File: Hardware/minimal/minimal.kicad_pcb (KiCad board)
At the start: 4 copper layers, 48 x 35 mm, 95 parts, among them J101 USB_C_Receptacle_USB2.0_16P, J301 AudioJack3_SwitchTR, J302 AudioJack3_SwitchTR, SW101 SW_SPST, U101 KTM1331TD-ST3, U102 USBLC6-2P6, U103 TLV76733DRVx, U104 TLV76733DRVx, U301 OPA2323, U302 TAC5242, U401 APS6404L-3SQRx-ZR, U402 RP2354A, Y401 ABM8-272-T3

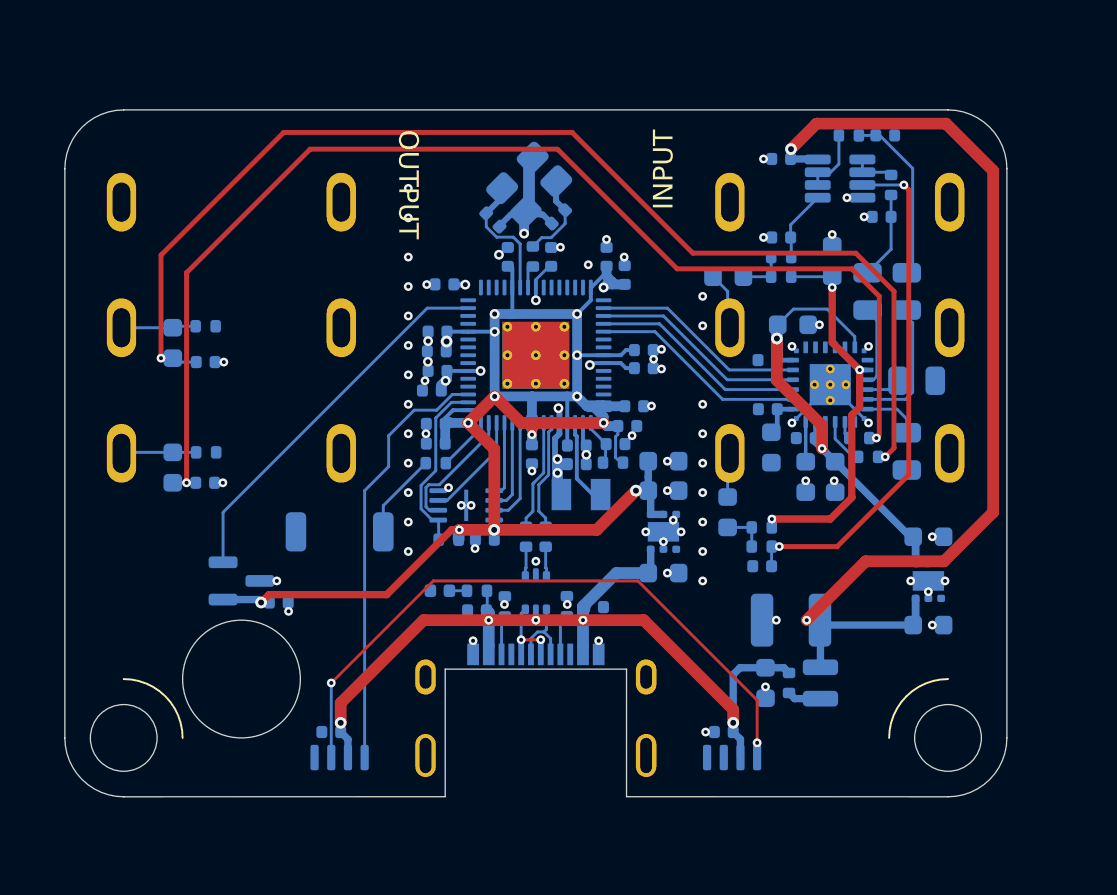
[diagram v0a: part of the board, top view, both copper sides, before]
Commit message: Commit DC-coupled TAC5112 design
This is a slightly modified 'minimal' board with the same board outline
but an added 3.5mm DC jack.

The upside: no coupling capacitors into the codec that have distortion
at low-end frequencies due to the capacitors' voltage coefficients.  The
existing 0805 4.7uF caps were large for this minimal board, and caused
the THD+N to go to roughly -65dB for a low-B bass signal at a reasonable
signal level of 0.1Vrms.  That's not horrible, but it's not optimal.

The 10Hz corner also caused issues for using the pedal as a measurement
instrument, since it introduced a consistent measurement error that was
initially incorrectly attributed to the pedal under test.

The other upside is simply the existence of the headphone jack.  That
user-visible addition is likely a lot more noticeable than the
low-frequency THD+N improvement this should bring or the improvement in
low-end frequency response.

Downside: the TAC212 with a better noise floor is out of stock, and so I
am back to the slightly lower dynamic range of the TAC5112 - but with
the new fixed footprint with proper paste and thermal vias.  The thermal
pad is likely to actually come into play now that the codec is used as a
headphone amplifier too.

The lower dynamic range is unlikely to be noticeable - it wasn't on the
original mono boards (the added noise was probably entirely due to the
negative inputs having been left floating on that board).

And I'll need to route i2c again, and it's an entirely new untested
configuration.  I've added a trace to route one of the TAC5112 GPIOs
just in case it comes in useful - possibly as an ASI error reporting
interrupt line.

The default codec routing for that new pin being routed is as an
interrupt output: driven low with a weak pull-up.  It's routed to GPIO15
on the rp2354, which hardware in turn defaults to a weak pull-down,
disconnected from any logic.

So without any firmware, this ends up being a few microamps of current
on that trace due to the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
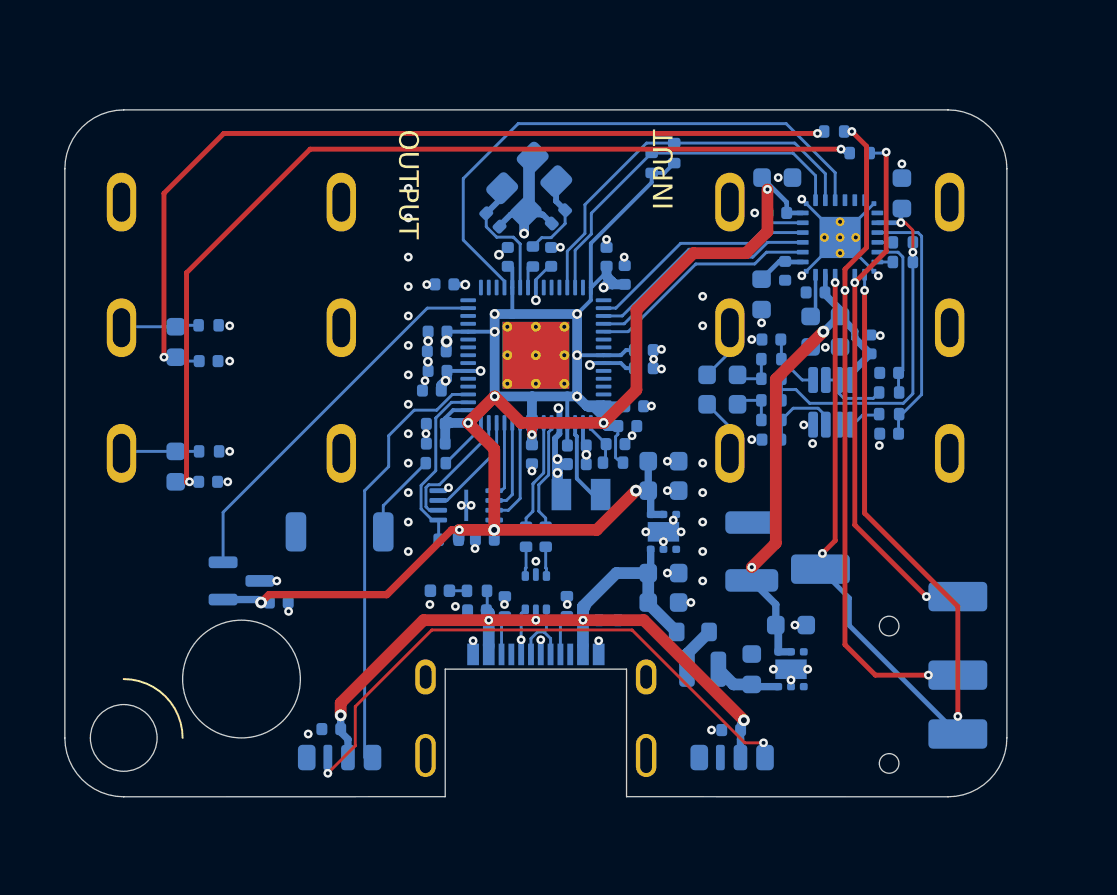
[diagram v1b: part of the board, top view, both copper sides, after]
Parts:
- removed C312, C313, C314, C315: 4.7uF, Capacitor_SMD:C_0805_2012Metric
- added J303: AudioJack4, Mylib:PJ-320D, B.Cu at (118.0, 135.0)
- added R105: 5k1, Resistor_SMD:R_0402_1005Metric, B.Cu at (105.9, 102.7)
- added R106: 5k1, Resistor_SMD:R_0402_1005Metric, B.Cu at (107.0, 102.2)
- added R312: 100R, Resistor_SMD:R_0402_1005Metric, B.Cu at (118.7, 107.8)
- added R313: 100R, Resistor_SMD:R_0402_1005Metric, B.Cu at (118.7, 106.8)
- D102, D103: value WS2812B-4020 -> WS2812B-4020-V6; footprint Mylib:WS2812B-4020 -> Mylib:WS2812B-4020-V6
- R104: value 10R -> 1R; footprint Resistor_SMD:R_0402_1005Metric -> Resistor_SMD:R_0603_1608Metric
- U302: value TAC5242 -> TAC5112
- moved R307 16.7 mm to (115.2, 101.1), turned to 180 degrees
- moved R301 14.5 mm to (116.5, 102.2), turned to 180 degrees
- moved R310 13.3 mm to (118.0, 114.4)
- moved C311 12.1 mm to (118.0, 113.4), turned to 0 degrees
- moved R309 11.7 mm to (118.0, 115.5), turned to 0 degrees
- moved U301 11.4 mm to (115.1, 114.9), turned to 90 degrees
- moved C310 11.1 mm to (118.0, 116.5)
- moved C301 10.5 mm to (117.0, 112.0), turned to -90 degrees
- moved C106 9.28 mm to (111.0, 128.5), turned to 90 degrees
- moved C109 8.32 mm to (113.0, 126.2)
- moved U103 8.32 mm to (113.0, 128.5)
- moved C317 7.82 mm to (111.5, 109.4)
- moved C316 7.54 mm to (112.3, 103.5)
- moved C322 7.52 mm to (112.3, 105.2)
- moved U302 7.52 mm to (115.5, 106.5)
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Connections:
- net /TAC5242/DREG renamed /TAC5212/DREG
- net /TAC5242/IN^{LEFT} renamed /TAC5212/IN^{LEFT}
- net /TAC5242/IN^{RIGHT} renamed /TAC5212/IN^{RIGHT}
- net /TAC5242/MICBIAS renamed /TAC5212/MICBIAS
- net /TAC5242/OUT^{LEFT} renamed /TAC5212/OUT^{LEFT}
- net /TAC5242/OUT^{RIGHT} renamed /TAC5212/OUT^{RIGHT}
- net /TAC5242/VREF renamed /TAC5212/VREF
- C105 pad 1: +5VA -> +3.3VA
- C106 pad 1: +5VA -> Net-(U103-IN)
- C301 pad 2: +5VA -> +3.3VA
- C310 pad 2: Net-(C310-Pad2) -> /TAC5212/IN1P
- C311 pad 2: Net-(C311-Pad2) -> /TAC5212/IN2P
- C316 pad 1: +3.3VA -> +3V3
- C322 pad 1: +3.3VA -> +3V3
- L101 pad 2: +5VA -> Net-(U103-IN)
- R309 pad 2: Net-(C310-Pad2) -> /TAC5212/IN1P
- R310 pad 2: Net-(C311-Pad2) -> /TAC5212/IN2P
- U103 pad 6: +5VA -> Net-(U103-IN)
- U301 pad 8: +5VA -> +3.3VA
- U302 pad 10: GND -> unconnected-(U302-GPIO2-Pad10)
- U302 pad 12: +3.3VA -> unconnected-(U302-GPI1-Pad12)
- U302 pad 15: /TAC5242/IN1P -> /TAC5212/IN1P
- U302 pad 16: /TAC5242/IN1M -> /TAC5212/IN1M
- U302 pad 17: /TAC5242/IN2P -> /TAC5212/IN2P
- U302 pad 18: /TAC5242/IN2M -> /TAC5212/IN2M
- U302 pad 19: unconnected-(U302-OUT1M-Pad19) -> /TAC5212/OUT1M
- U302 pad 22: unconnected-(U302-OUT2M-Pad22) -> /TAC5212/OUT1M
- U302 pad 6: +3.3VA -> +3V3
- U302 pad 7: GND -> /RP2354/GPIO17
- U302 pad 8: GND -> /RP2354/GPIO16
- U302 pad 9: GND -> /RP2354/GPIO15
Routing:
- net /TAC5212/OUT1M: track 0.00 -> 52.0 mm, vias 0 -> 4
- net +5VA: track 51.4 -> 0.00 mm, vias 2 -> 0
- net /OUT2P: track 2.41 -> 34.5 mm, vias 0 -> 3
- net /RP2354/GPIO15: track 0.00 -> 29.0 mm
- net +3V3: track 117.8 -> 146.2 mm, vias 16 -> 17
- net /OUT1P: track 0.91 -> 27.7 mm, vias 0 -> 3
- net Net-(U301A-+): track 26.5 -> 4.13 mm, vias 2 -> 0
- net /RP2354/GPIO16: track 0.00 -> 20.1 mm
- net /RP2354/GPIO17: track 0.00 -> 18.6 mm
- net Net-(C308-Pad2): track 58.7 -> 44.8 mm
- net /TAC5212/IN1P: track 0.00 -> 13.0 mm
- net Net-(C302-Pad2): track 60.2 -> 48.4 mm
- net Net-(C311-Pad2): track 8.88 -> 0.00 mm
- net /TAC5212/IN2P: track 0.00 -> 8.47 mm
- net /TAC5242/IN2P: track 6.76 -> 0.00 mm
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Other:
- outline, holes or cut-outs redrawn
